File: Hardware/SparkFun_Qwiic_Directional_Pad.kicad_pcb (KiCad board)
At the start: 2 copper layers, 25.4 x 25.4 mm, 66 parts, among them J1 Qwiic_RA, J2 Conn_01x04, J3 Qwiic_RA, J5 I2C, SW2 Nav Switch, U4 PCA9557PW

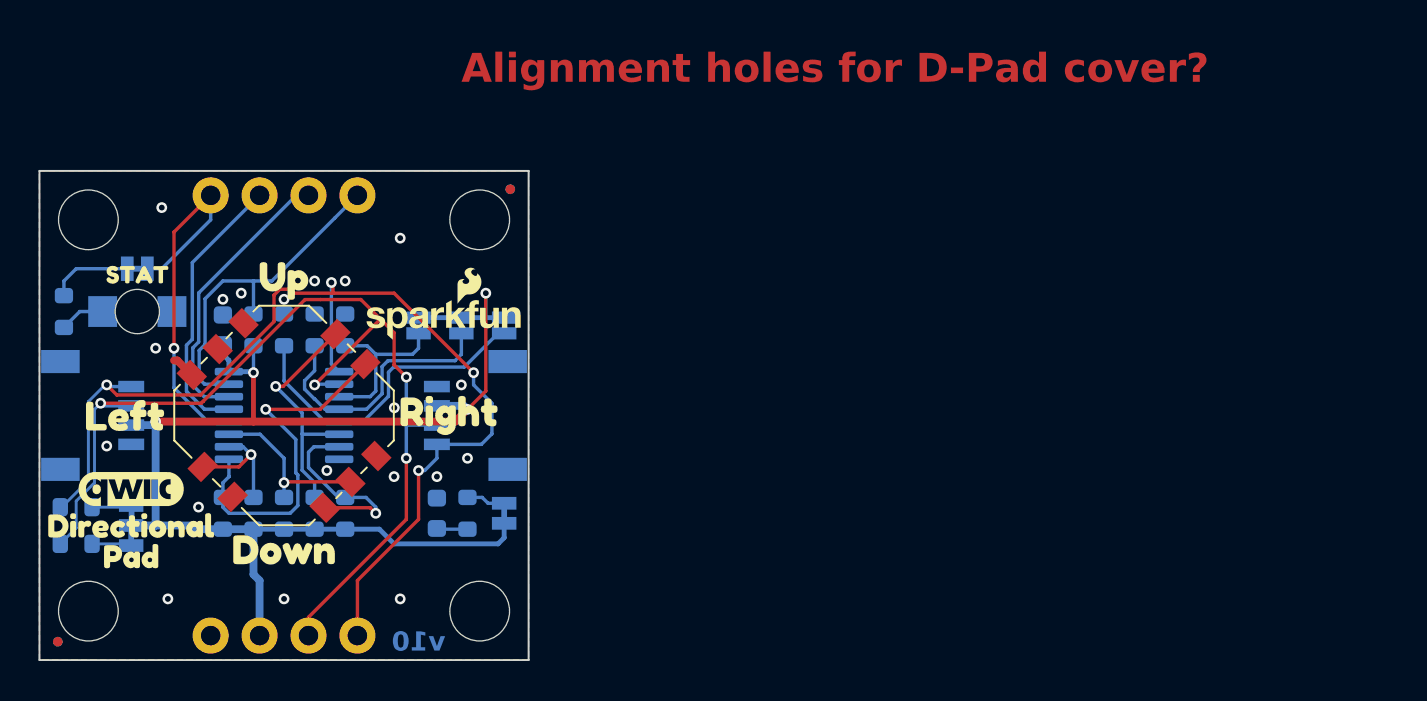
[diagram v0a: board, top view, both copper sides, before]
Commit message: Switch to RGB 1205 rear mount LED
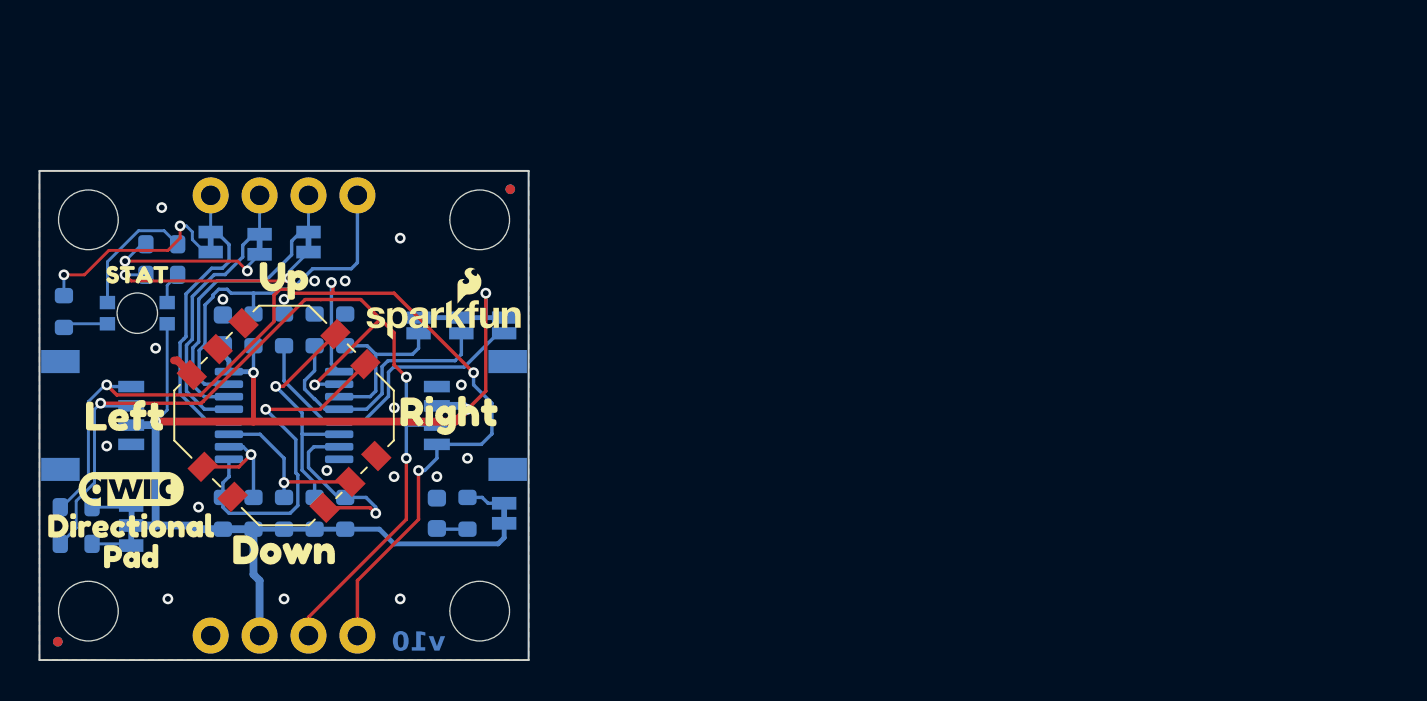
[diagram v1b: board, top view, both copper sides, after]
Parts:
- removed D4: Green, SparkFun-LED:LED_1206_Bottom_Green
- removed kibuzzard-66EF7907: G***, kibuzzard-66EF7907
- removed kibuzzard-66EF7923: G***, kibuzzard-66EF7923
- removed kibuzzard-66EF793A: G***, kibuzzard-66EF793A
- removed kibuzzard-66EF7940: G***, kibuzzard-66EF7940
- added D2: LED_RGB, SparkFun-LED:LED_1205_RGB_Bottom, B.Cu at (140.3, 99.5)
- added JP7: 6, SparkFun-Jumper:Jumper_2_NC_Trace, B.Cu at (146.7, 95.9)
- added JP8: 7, SparkFun-Jumper:Jumper_2_NC_Trace, B.Cu at (149.2, 95.8)
- added R14: 2.2k, SparkFun-Resistor:R_0603_1608Metric, B.Cu at (141.6, 95.9)
- added R15: 1k, SparkFun-Resistor:R_0603_1608Metric, B.Cu at (141.6, 97.5)
- added kibuzzard-66F18F5E: G***, kibuzzard-66F18F5E, B.Cu at (144.1, 97.8)
- added kibuzzard-66F18F8F: G***, kibuzzard-66F18F8F, B.Cu at (146.7, 97.8)
- added kibuzzard-66F18F9B: G***, kibuzzard-66F18F9B, B.Cu at (149.2, 97.7)
- JP5: value STAT -> 5
- moved kibuzzard-66EF5827 7.62 mm to (151.8, 96.5)
- moved JP5 4.05 mm to (144.1, 95.8), turned to 90 degrees
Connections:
- net IO5/STAT renamed IO5/Red
- net IO6 renamed IO6/Green
- net IO7 renamed IO7/Blue
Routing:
- net Net-(JP8-A): track 0.00 -> 11.6 mm, vias 0 -> 2
- net Net-(JP7-A): track 0.00 -> 9.13 mm, vias 0 -> 2
- net Net-(D2-GK): track 0.00 -> 6.72 mm
- net Net-(JP5-A): track 4.31 -> 10.9 mm, vias 0 -> 2
- net 3.3V: track 70.1 -> 75.4 mm
- net IO5/Red: track 20.0 -> 15.4 mm, vias 1 -> 0
- net IO7/Blue: track 15.5 -> 17.5 mm
- net Net-(D2-BK): track 0.00 -> 1.67 mm
- net ~{RESET}: track 17.8 -> 19.3 mm
- net IO6/Green: track 14.3 -> 15.2 mm
- net GND: vias 19 -> 18
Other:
- board text removed: "Alignment holes for D-Pad cover?"

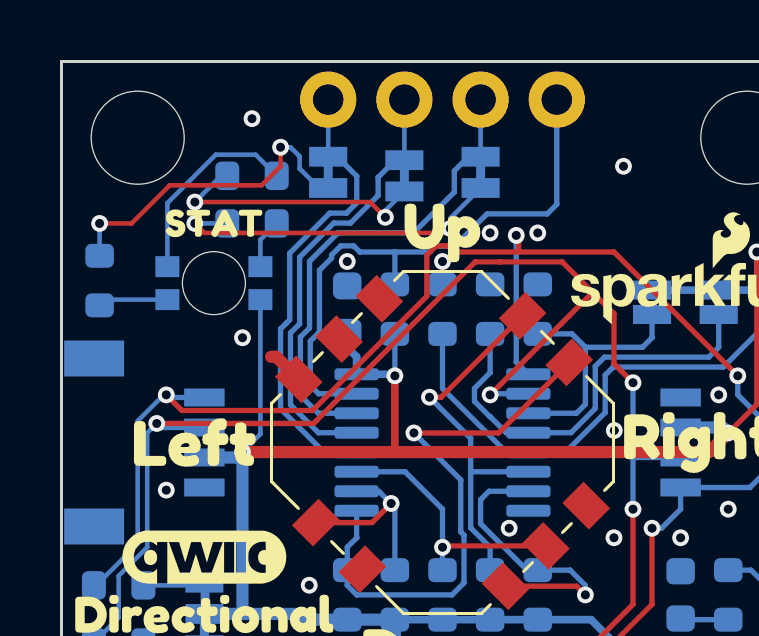
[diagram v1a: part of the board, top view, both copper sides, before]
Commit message: Switch to PCA9554
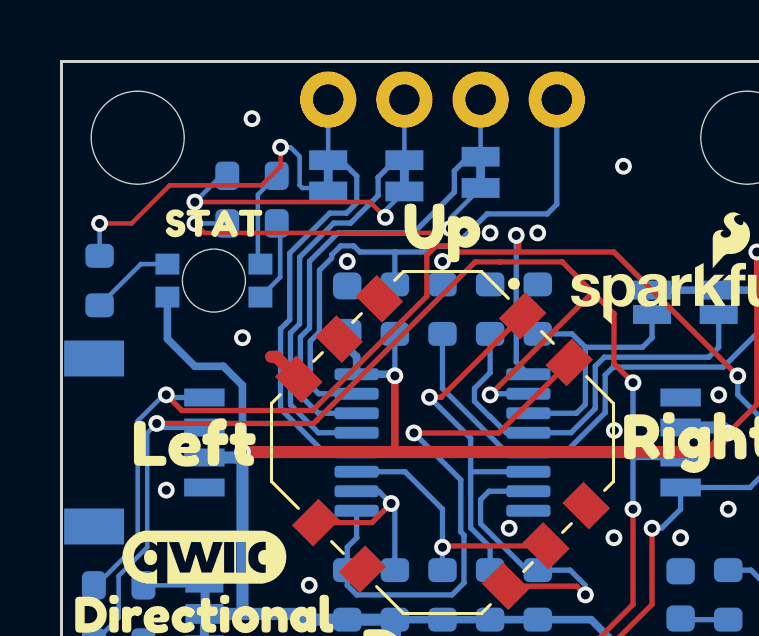
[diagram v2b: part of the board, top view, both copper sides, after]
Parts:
- G***: footprint SparkFun-Aesthetic:SparkFun_Logo_NoFlame_8mm -> SparkFun-Aesthetic:SparkFun_Logo_8mm
- moved G*** 0.43 mm to (143.5, 104.8)
- moved JP5 0.11 mm to (144.1, 95.9)
- moved D2 0.09 mm to (140.3, 99.4), turned to 0 degrees
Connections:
- net IO5/Red renamed IO5/Blue
- net IO7/Blue renamed IO7/Red
- R15 pad 2: Net-(D2-BK) -> Net-(D2-RK)
- R6 pad 2: Net-(D2-RK) -> Net-(D2-BK)
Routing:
- net Net-(D2-GK): track 6.72 -> 3.24 mm
- net 3.3V: track 75.4 -> 76.8 mm
- net Net-(D2-BK): track 1.67 -> 2.83 mm

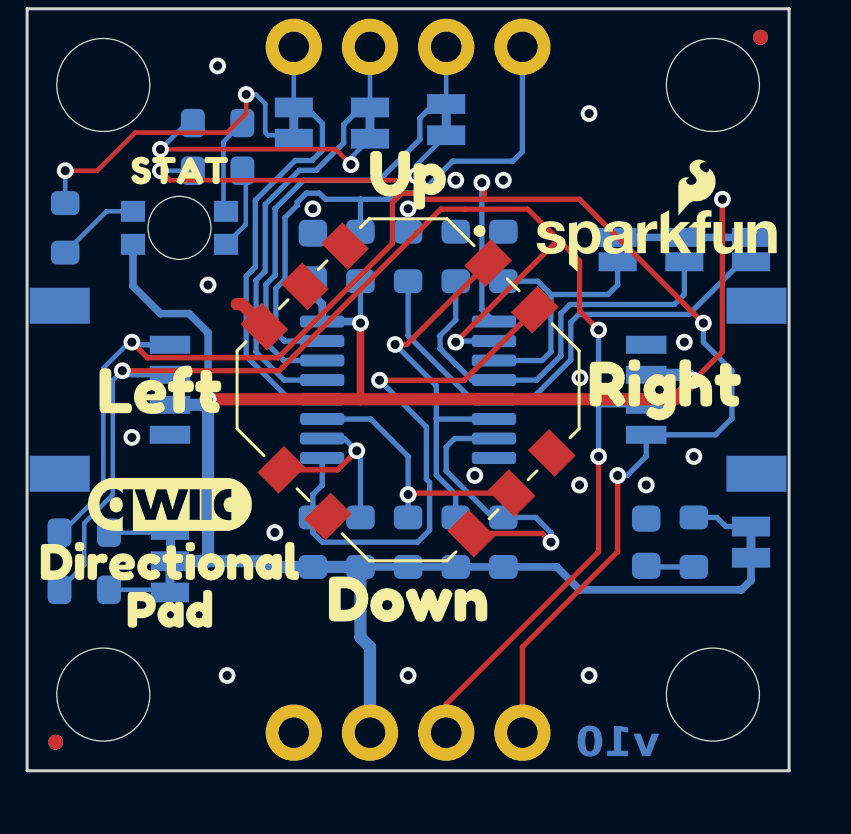
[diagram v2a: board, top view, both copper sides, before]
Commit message: Switch to PCA9554 with INT pin
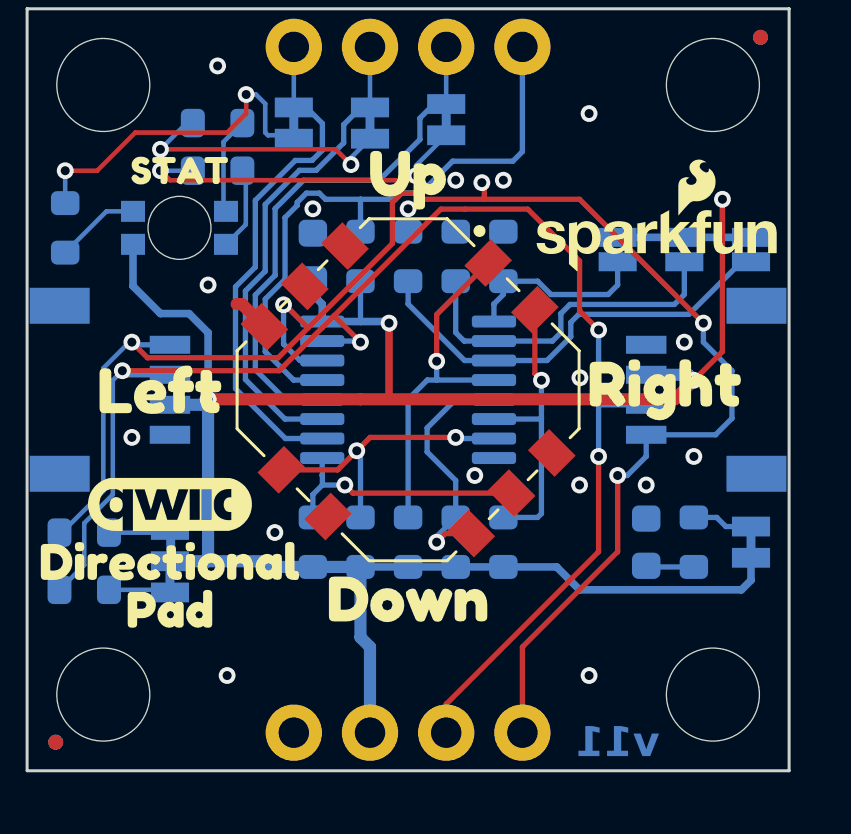
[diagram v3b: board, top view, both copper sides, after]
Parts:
- removed kibuzzard-66EF5827: G***, kibuzzard-66EF5827
- added kibuzzard-67117BDD: G***, kibuzzard-67117BDD, B.Cu at (151.8, 95.6)
- U4: value PCA9557PW -> PCA9554PW
- moved R10 6.35 mm to (151.1, 109.9)
- moved R12 3.18 mm to (144.8, 109.9)
- moved R8 1.59 mm to (149.5, 109.9)
- moved R9 1.59 mm to (148.0, 109.9)
- moved kibuzzard-66F18F9B 0.11 mm to (149.2, 97.8)
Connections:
- J2 pad 4: ~{RESET} -> ~{INT}
- R4 pad 1: ~{RESET} -> ~{INT}
- U4 pad 1: SCL -> ADR0
- U4 pad 10: SW_Left -> IO5/Blue
- U4 pad 11: SW_Center -> IO6/Green
- U4 pad 12: IO5/Blue -> IO7/Red
- U4 pad 13: IO6/Green -> ~{INT}
- U4 pad 14: IO7/Red -> SCL
- U4 pad 15: ~{RESET} -> SDA
- U4 pad 2: SDA -> ADR1
- U4 pad 3: ADR0 -> ADR2
- U4 pad 4: ADR1 -> SW_Up
- U4 pad 5: ADR2 -> SW_Down
- U4 pad 6: SW_Up -> SW_Right
- U4 pad 7: SW_Down -> SW_Left
- U4 pad 9: SW_Right -> SW_Center
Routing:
- net ~{INT}: track 0.00 -> 20.7 mm
- net ~{RESET}: track 19.3 -> 0.00 mm
- net SW_Right: track 18.7 -> 9.80 mm
- net SDA: track 53.8 -> 50.2 mm
- net SW_Left: track 6.37 -> 9.64 mm, vias 1 -> 2
- net ADR1: track 14.1 -> 11.6 mm
- net ADR0: track 8.83 -> 6.38 mm
- net ADR2: track 16.8 -> 14.6 mm
- net IO5/Blue: track 15.4 -> 17.1 mm
- net SW_Down: track 9.95 -> 8.36 mm
- net IO6/Green: track 15.2 -> 16.8 mm
- net IO7/Red: track 17.5 -> 19.0 mm
- net SW_Up: track 12.8 -> 11.7 mm
- net 3.3V: track 76.8 -> 77.7 mm
- net SCL: track 56.9 -> 56.0 mm, vias 4 -> 5
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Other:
- board text added: "v11"
- board text removed: "v10"

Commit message: Update jumper names, I2C address table.
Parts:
- JP1: value ~ -> A0
- JP2: value ~ -> A1
- JP3: value ~ -> A2
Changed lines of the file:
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@@
 			)
 		)
-		(property "Value" "~"
+		(property "Value" "A0"
 			(at 0 -1.143 90)
 			(layer "B.Fab")
@@
 			)
 		)
-		(property "Value" "~"
+		(property "Value" "A1"
 			(at 0 -1.143 90)
 			(layer "B.Fab")
@@
 				(font
 					(size 0.001 0.001)
+					(thickness 0.15)
 				)
 				(justify mirror)
@@
 				(font
 					(size 0.001 0.001)
+					(thickness 0.15)
 				)
 				(justify mirror)
@@
 			)
 		)
-		(property "Value" "~"
+		(property "Value" "A2"
 			(at 0 -1.143 90)
 			(layer "B.Fab")
